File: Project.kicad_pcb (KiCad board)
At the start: 2 copper layers, 2 parts, among them U1 ESP32-DEVKITC-32D

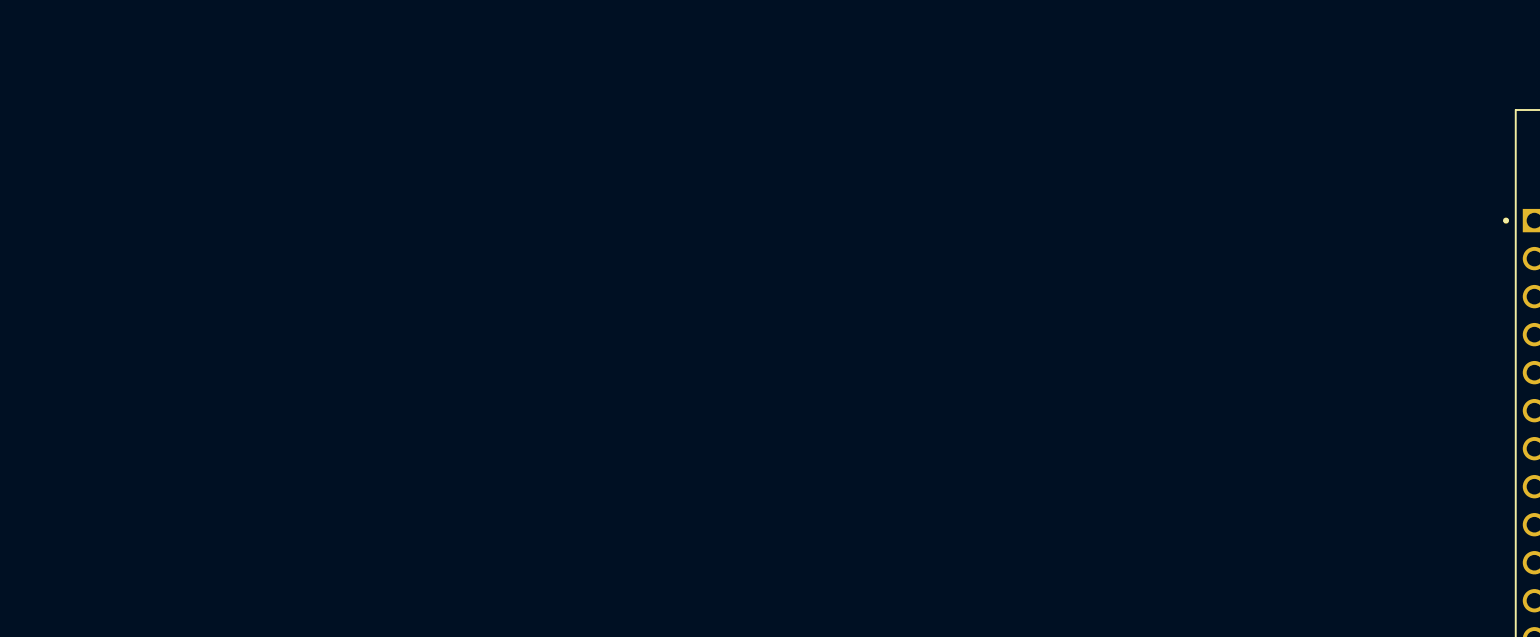
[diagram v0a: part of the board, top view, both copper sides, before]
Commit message: Changed devboard to mcu
-Changed devboard to standalone mcu
-added 5v to 3.3v stabilizer
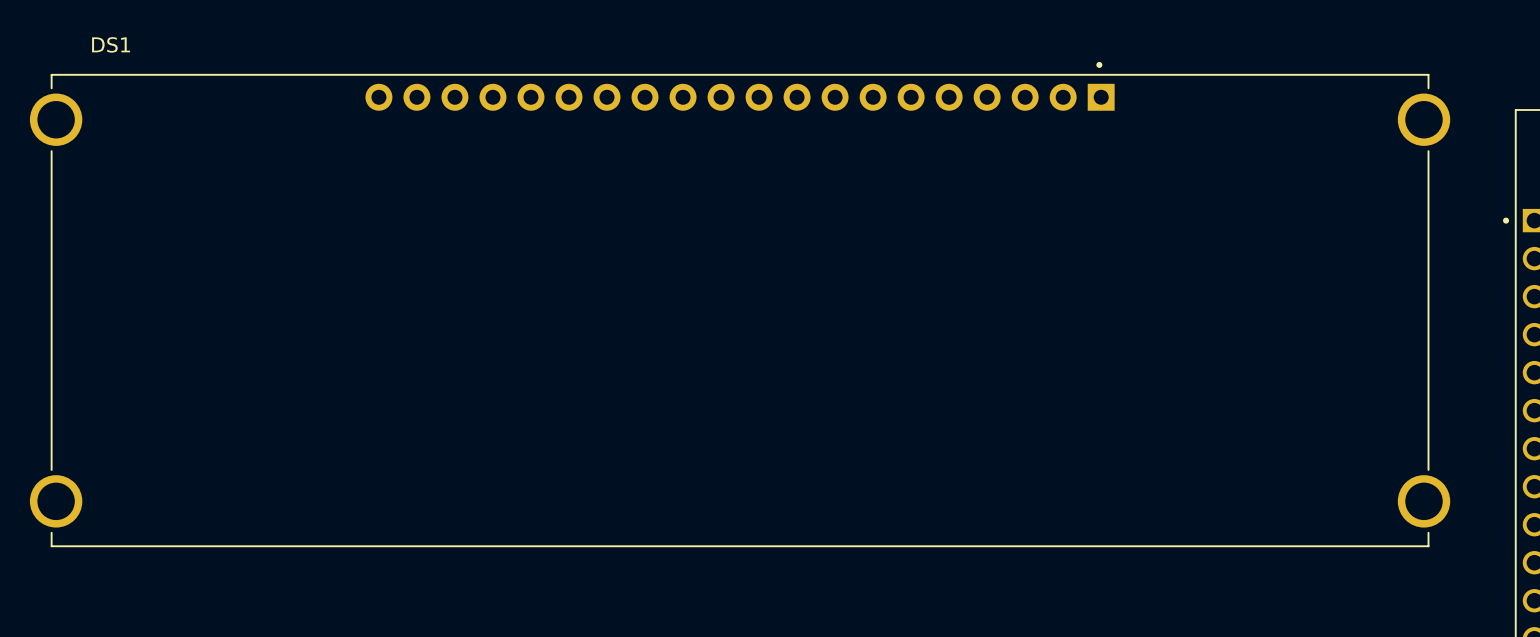
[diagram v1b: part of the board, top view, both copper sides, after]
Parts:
- added DS1: NHD-0420CW-AB3, NHD-0420CW-AB3:LCD_NHD-0420CW-AB3, F.Cu at (80.3, 68.2)
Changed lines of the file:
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@@
   (net 41 "unconnected-(U1-SD0-PadJ3-18)")
   (net 42 "unconnected-(U1-CLK-PadJ3-19)")
+  (net 43 "Net-(DS1-VSS-Pad1)")
+  (net 44 "unconnected-(DS1-VDD-Pad2)")
+  (net 45 "unconnected-(DS1-REGVDD-Pad3)")
+  (net 46 "unconnected-(DS1-D{slash}C{slash}NC{slash}SA0-Pad4)")
+  (net 47 "unconnected-(DS1-R{slash}W{slash}NC-Pad5)")
+  (net 48 "unconnected-(DS1-E{slash}NC-Pad6)")
+  (net 49 "unconnected-(DS1-DB0{slash}SCLK{slash}SCL-Pad7)")
+  (net 50 "unconnected-(DS1-DB1{slash}SDI{slash}SDAIN-Pad8)")
+  (net 51 "unconnected-(DS1-DB2{slash}SDO{slash}SDAOUT-Pad9)")
+  (net 52 "unconnected-(DS1-DB3{slash}NC-Pad10)")
+  (net 53 "unconnected-(DS1-DB4{slash}NC-Pad11)")
+  (net 54 "unconnected-(DS1-DB5{slash}NC-Pad12)")
+  (net 55 "unconnected-(DS1-DB6{slash}NC-Pad13)")
+  (net 56 "unconnected-(DS1-DB7{slash}NC-Pad14)")
+  (net 57 "unconnected-(DS1-~{CS}{slash}NC-Pad15)")
+  (net 58 "unconnected-(DS1-~{RES}-Pad16)")
+  (net 59 "unconnected-(DS1-BS0-Pad17)")
+  (net 60 "unconnected-(DS1-BS1-Pad18)")
+  (net 61 "unconnected-(DS1-BS2-Pad19)")
   (footprint "ESP32-DEVKITC-32D:MODULE_ESP32-DEVKITC-32D" (layer "F.Cu")
     (at 146.08 82)
@@
       (net 42 "unconnected-(U1-CLK-PadJ3-19)") (pinfunction "CLK") (pintype "input") (solder_mask_margin 0.102))
   )
+  (footprint "NHD-0420CW-AB3:LCD_NHD-0420CW-AB3" (layer "F.Cu")
+    (at 80.3 68.25)
+    (property "Check_prices" "https://www.snapeda.com/parts/NHD-0420CW-AB3/Newhaven+Display+Intl/view-part/?ref=eda")
+    (property "Description" "\nCharacter OLED;4x20;920x31.5;Char OLED Module;Blue;4/8-bit Parallel, SPI, I2C | Newhaven Display International NHD-0420CW-AB3\n")
+    (property "MANUFACTURER" "Newhaven Display Intl")
+    (property "MAXIMUM_PACKAGE_HEIGHT" "7 mm")
+    (property "MF" "Newhaven Display")
+    (property "MP" "NHD-0420CW-AB3")
+    (property "PARTREV" "5")
+    (property "Package" "None")
+    (property "RS_Components_70518327_Purchase_URL" "https://www.snapeda.com/api/url_track_click/https%253A//us.rs-online.com/product/newhaven-display-international/nhd-0420cw-ab3/70518327/%253Futm_source%253DSnapEDA%2526utm_medium%253Dpart_sourcing%2526utm_campaign%253Dpartsourcing_SnapEDA_IMP_EX_GR/?unipart_id=1161384&manufacturer=Newhaven Display&part_name=NHD-0420CW-AB3&search_term=display 4x20")
+    (property "STANDARD" "Manufacturer Recommendation")
+    (property "Sheetfile" "Project.kicad_sch")
+    (property "Sheetname" "")
+    (property "SnapEDA_Link" "https://www.snapeda.com/parts/NHD-0420CW-AB3/Newhaven+Display+Intl/view-part/?ref=snap")
+    (attr through_hole)
+    (fp_text reference "DS1" (at -42.035 -17.715) (layer "F.SilkS")
+        (effects (font (size 1 1) (thickness 0.15)))
+    )
+    (fp_text value "NHD-0420CW-AB3" (at -33.78 17.305) (layer "F.Fab")
+        (effects (font (size 1 1) (thickness 0.15)))
+    )
+    (fp_line (start -46 -15.75) (end -46 -14.85)
+      (stroke (width 0.127) (type solid)) (layer "F.SilkS"))
+    (fp_line (start -46 10.65) (end -46 -10.65)
+      (stroke (width 0.127) (type solid)) (layer "F.SilkS"))
+    (fp_line (start -46 14.85) (end -46 15.75)
+      (stroke (width 0.127) (type solid)) (layer "F.SilkS"))
+    (fp_line (start -46 15.75) (end 46 15.75)
+      (stroke (width 0.127) (type solid)) (layer "F.SilkS"))
+    (fp_line (start 46 -15.75) (end -46 -15.75)
+      (stroke (width 0.127) (type solid)) (layer "F.SilkS"))
+    (fp_line (start 46 -14.85) (end 46 -15.75)
+      (stroke (width 0.127) (type solid)) (layer "F.SilkS"))
+    (fp_line (start 46 -10.65) (end 46 10.65)
+      (stroke (width 0.127) (type solid)) (layer "F.SilkS"))
+    (fp_line (start 46 15.75) (end 46 14.85)
+      (stroke (width 0.127) (type solid)) (layer "F.SilkS"))
+    (fp_circle (center 24.01 -16.411) (end 24.11 -16.411)
+      (stroke (width 0.2) (type solid)) (fill none) (layer "F.SilkS"))
+    (fp_line (start -47.7 -16) (end -47.7 16)
+      (stroke (width 0.05) (type solid)) (layer "F.CrtYd"))
+    (fp_line (start -47.7 16) (end 47.7 16)
+      (stroke (width 0.05) (type solid)) (layer "F.CrtYd"))
+    (fp_line (start 47.7 -16) (end -47.7 -16)
+      (stroke (width 0.05) (type solid)) (layer "F.CrtYd"))
+    (fp_line (start 47.7 16) (end 47.7 -16)
+      (stroke (width 0.05) (type solid)) (layer "F.CrtYd"))
+    (fp_line (start -46 -15.75) (end 46 -15.75)
+      (stroke (width 0.127) (type solid)) (layer "F.Fab"))
+    (fp_line (start -46 15.75) (end -46 -15.75)
+      (stroke (width 0.127) (type solid)) (layer "F.Fab"))
+    (fp_line (start 46 -15.75) (end 46 15.75)
+      (stroke (width 0.127) (type solid)) (layer "F.Fab"))
+    (fp_line (start 46 15.75) (end -46 15.75)
+      (stroke (width 0.127) (type solid)) (layer "F.Fab"))
+    (fp_circle (center 24.01 -16.411) (end 24.11 -16.411)
+      (stroke (width 0.2) (type solid)) (fill none) (layer "F.Fab"))
+    (pad "1" thru_hole rect (at 24.13 -14.25) (size 1.8 1.8) (drill 1) (layers "*.Cu" "*.Mask")
+      (net 43 "Net-(DS1-VSS-Pad1)") (pinfunction "VSS") (pintype "power_in") (solder_mask_margin 0.102))
+    (pad "2" thru_hole circle (at 21.59 -14.25) (size 1.8 1.8) (drill 1) (layers "*.Cu" "*.Mask")
+      (net 44 "unconnected-(DS1-VDD-Pad2)") (pinfunction "VDD") (pintype "power_in") (solder_mask_margin 0.102))
+    (pad "3" thru_hole circle (at 19.05 -14.25) (size 1.8 1.8) (drill 1) (layers "*.Cu" "*.Mask")
+      (net 45 "unconnected-(DS1-REGVDD-Pad3)") (pinfunction "REGVDD") (pintype "power_in") (solder_mask_margin 0.102))
+    (pad "4" thru_hole circle (at 16.51 -14.25) (size 1.8 1.8) (drill 1) (layers "*.Cu" "*.Mask")
+      (net 46 "unconnected-(DS1-D{slash}C{slash}NC{slash}SA0-Pad4)") (pinfunction "D/C/NC/SA0") (pintype "bidirectional") (solder_mask_margin 0.102))
+    (pad "5" thru_hole circle (at 13.97 -14.25) (size 1.8 1.8) (drill 1) (layers "*.Cu" "*.Mask")
+      (net 47 "unconnected-(DS1-R{slash}W{slash}NC-Pad5)") (pinfunction "R/W/NC") (pintype "bidirectional") (solder_mask_margin 0.102))
+    (pad "6" thru_hole circle (at 11.43 -14.25) (size 1.8 1.8) (drill 1) (layers "*.Cu" "*.Mask")
+      (net 48 "unconnected-(DS1-E{slash}NC-Pad6)") (pinfunction "E/NC") (pintype "bidirectional") (solder_mask_margin 0.102))
+    (pad "7" thru_hole circle (at 8.89 -14.25) (size 1.8 1.8) (drill 1) (layers "*.Cu" "*.Mask")
+      (net 49 "unconnected-(DS1-DB0{slash}SCLK{slash}SCL-Pad7)") (pinfunction "DB0/SCLK/SCL") (pintype "bidirectional") (solder_mask_margin 0.102))
+    (pad "8" thru_hole circle (at 6.35 -14.25) (size 1.8 1.8) (drill 1) (layers "*.Cu" "*.Mask")
+      (net 50 "unconnected-(DS1-DB1{slash}SDI{slash}SDAIN-Pad8)") (pinfunction "DB1/SDI/SDAIN") (pintype "bidirectional") (solder_mask_margin 0.102))
+    (pad "9" thru_hole circle (at 3.81 -14.25) (size 1.8 1.8) (drill 1) (layers "*.Cu" "*.Mask")
+      (net 51 "unconnected-(DS1-DB2{slash}SDO{slash}SDAOUT-Pad9)") (pinfunction "DB2/SDO/SDAOUT") (pintype "bidirectional") (solder_mask_margin 0.102))
+    (pad "10" thru_hole circle (at 1.27 -14.25) (size 1.8 1.8) (drill 1) (layers "*.Cu" "*.Mask")
+      (net 52 "unconnected-(DS1-DB3{slash}NC-Pad10)") (pinfunction "DB3/NC") (pintype "bidirectional") (solder_mask_margin 0.102))
+    (pad "11" thru_hole circle (at -1.27 -14.25) (size 1.8 1.8) (drill 1) (layers "*.Cu" "*.Mask")
+      (net 53 "unconnected-(DS1-DB4{slash}NC-Pad11)") (pinfunction "DB4/NC") (pintype "bidirectional") (solder_mask_margin 0.102))
+    (pad "12" thru_hole circle (at -3.81 -14.25) (size 1.8 1.8) (drill 1) (layers "*.Cu" "*.Mask")
+      (net 54 "unconnected-(DS1-DB5{slash}NC-Pad12)") (pinfunction "DB5/NC") (pintype "bidirectional") (solder_mask_margin 0.102))
+    (pad "13" thru_hole circle (at -6.35 -14.25) (size 1.8 1.8) (drill 1) (layers "*.Cu" "*.Mask")
+      (net 55 "unconnected-(DS1-DB6{slash}NC-Pad13)") (pinfunction "DB6/NC") (pintype "bidirectional") (solder_mask_margin 0.102))
+    (pad "14" thru_hole circle (at -8.89 -14.25) (size 1.8 1.8) (drill 1) (layers "*.Cu" "*.Mask")
+      (net 56 "unconnected-(DS1-DB7{slash}NC-Pad14)") (pinfunction "DB7/NC") (pintype "bidirectional") (solder_mask_margin 0.102))
+    (pad "15" thru_hole circle (at -11.43 -14.25) (size 1.8 1.8) (drill 1) (layers "*.Cu" "*.Mask")
+      (net 57 "unconnected-(DS1-~{CS}{slash}NC-Pad15)") (pinfunction "~{CS}/NC") (pintype "passive") (solder_mask_margin 0.102))
+    (pad "16" thru_hole circle (at -13.97 -14.25) (size 1.8 1.8) (drill 1) (layers "*.Cu" "*.Mask")
+      (net 58 "unconnected-(DS1-~{RES}-Pad16)") (pinfunction "~{RES}") (pintype "input") (solder_mask_margin 0.102))
+    (pad "17" thru_hole circle (at -16.51 -14.25) (size 1.8 1.8) (drill 1) (layers "*.Cu" "*.Mask")
+      (net 59 "unconnected-(DS1-BS0-Pad17)") (pinfunction "BS0") (pintype "input") (solder_mask_margin 0.102))
+    (pad "18" thru_hole circle (at -19.05 -14.25) (size 1.8 1.8) (drill 1) (layers "*.Cu" "*.Mask")
+      (net 60 "unconnected-(DS1-BS1-Pad18)") (pinfunction "BS1") (pintype "input") (solder_mask_margin 0.102))
+    (pad "19" thru_hole circle (at -21.59 -14.25) (size 1.8 1.8) (drill 1) (layers "*.Cu" "*.Mask")
+      (net 61 "unconnected-(DS1-BS2-Pad19)") (pinfunction "BS2") (pintype "input") (solder_mask_margin 0.102))
+    (pad "20" thru_hole circle (at -24.13 -14.25) (size 1.8 1.8) (drill 1) (layers "*.Cu" "*.Mask")
+      (net 43 "Net-(DS1-VSS-Pad1)") (pinfunction "VSS") (pintype "power_in") (solder_mask_margin 0.102))
+    (pad "SH1" thru_hole circle (at -45.7 -12.75) (size 3.5 3.5) (drill 2.5) (layers "*.Cu" "*.Mask")
+      (solder_mask_margin 0.102))
+    (pad "SH2" thru_hole circle (at 45.7 -12.75) (size 3.5 3.5) (drill 2.5) (layers "*.Cu" "*.Mask")
+      (solder_mask_margin 0.102))
+    (pad "SH3" thru_hole circle (at 45.7 12.75) (size 3.5 3.5) (drill 2.5) (layers "*.Cu" "*.Mask")
+      (solder_mask_margin 0.102))
+    (pad "SH4" thru_hole circle (at -45.7 12.75) (size 3.5 3.5) (drill 2.5) (layers "*.Cu" "*.Mask")
+      (solder_mask_margin 0.102))
+  )
   (footprint "PSK-S25B-5-PB:CONV_PSK-S25B-5-PB" (layer "F.Cu")
